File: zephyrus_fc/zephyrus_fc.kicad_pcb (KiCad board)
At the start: 4 copper layers, 92.7 x 43.2 mm, 58 parts, among them J1 SWD_interface, J10 Conn_02x20_Counter_Clockwise, J11 Conn_02x04_Counter_Clockwise, J2 POWER, J3 SERVO1, J4 SERVO2, J5 SERVO3, J6 SERVO4, J7 SERVO5, J8 IBUS_RX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

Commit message: ready to order
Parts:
- added J12: GPS_UART, Connector_PinHeader_2.54mm:PinHeader_1x06_P2.54mm_Vertical, F.Cu at (119.4, 64.0)
- added J13: USART2, Connector_PinHeader_2.54mm:PinHeader_1x06_P2.54mm_Vertical, F.Cu at (123.2, 64.0)
- added J15: Conn_01x04, Connector_PinHeader_2.54mm:PinHeader_1x04_P2.54mm_Vertical, F.Cu at (130.6, 64.0)
- added J16: Conn_01x04, Connector_PinHeader_2.54mm:PinHeader_1x04_P2.54mm_Vertical, F.Cu at (126.8, 64.0)
- added R11: 2.2k, Resistor_SMD:R_0402_1005Metric, F.Cu at (119.9, 57.9)
- added R12: 2.2k, Resistor_SMD:R_0402_1005Metric, F.Cu at (118.6, 57.9)
- added R13: 2.2k, Resistor_SMD:R_0402_1005Metric, F.Cu at (117.3, 57.9)
- added R14: 2.2k, Resistor_SMD:R_0402_1005Metric, F.Cu at (116.1, 57.9)
- added R7: 2.2k, Resistor_SMD:R_0402_1005Metric, F.Cu at (114.8, 57.9)
- added R8: 2.2k, Resistor_SMD:R_0402_1005Metric, F.Cu at (113.5, 57.9)
- moved J5 75.0 mm to (192.0, 63.9), turned to -90 degrees
- moved J3 74.7 mm to (182.4, 63.8), turned to -90 degrees
- moved J6 68.4 mm to (192.0, 68.5), turned to -90 degrees
- moved J4 68.1 mm to (182.4, 68.5), turned to -90 degrees
- moved J7 61.8 mm to (192.0, 73.2), turned to -90 degrees
- moved J8 55.2 mm to (192.0, 77.8), turned to -90 degrees
- moved J2 48.4 mm to (192.0, 82.3), turned to -90 degrees
- moved D1 31.1 mm to (106.4, 87.9)
- moved R2 31.1 mm to (109.2, 87.9)
- moved J1 20.7 mm to (172.2, 73.2), turned to 90 degrees
- moved U5 11.3 mm to (108.0, 65.0), turned to 0 degrees
- moved C26 11.1 mm to (178.8, 75.4), turned to 180 degrees
- moved R6 10.5 mm to (178.8, 76.7), turned to 0 degrees
- moved R5 10.1 mm to (178.8, 78.0), turned to 180 degrees
- moved C23 5.63 mm to (113.6, 66.8), turned to 0 degrees
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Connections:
- net /PB10 renamed /I2C2_SCL
- net /PB11 renamed /I2C2_SDA
- net /PB8 renamed /I2C1_SCL
- net /PB9 renamed /I2C1_SDA
- net /PD12 renamed /I2C4_SCL
- net /PD13 renamed /I2C4_SDA
- net VCC renamed +5V
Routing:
- net +5V: track 17.5 -> 197.9 mm, vias 0 -> 3
- net /I2C1_SCL: track 34.4 -> 100.9 mm
- net /PA8: track 24.3 -> 90.1 mm
- net /PA9: track 20.3 -> 82.9 mm, vias 0 -> 3
- net /I2C1_SDA: track 33.0 -> 92.9 mm, vias 1 -> 2
- net /PC6: track 27.3 -> 84.4 mm, vias 0 -> 3
- net /PA13: track 19.9 -> 74.6 mm, vias 1 -> 2
- net /PA14: track 12.7 -> 67.0 mm, vias 0 -> 2
- net /PC7: track 23.4 -> 76.0 mm, vias 0 -> 3
- net /PE0: track 32.8 -> 73.2 mm, vias 1 -> 3
- net /PB6: track 22.3 -> 60.5 mm
- net /I2C4_SCL: track 31.2 -> 68.9 mm, vias 0 -> 1
- net /PE1: track 30.6 -> 68.1 mm, vias 1 -> 3
- net /I2C2_SCL: track 16.8 -> 53.8 mm
- net /PD3: track 17.4 -> 53.5 mm, vias 0 -> 1
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
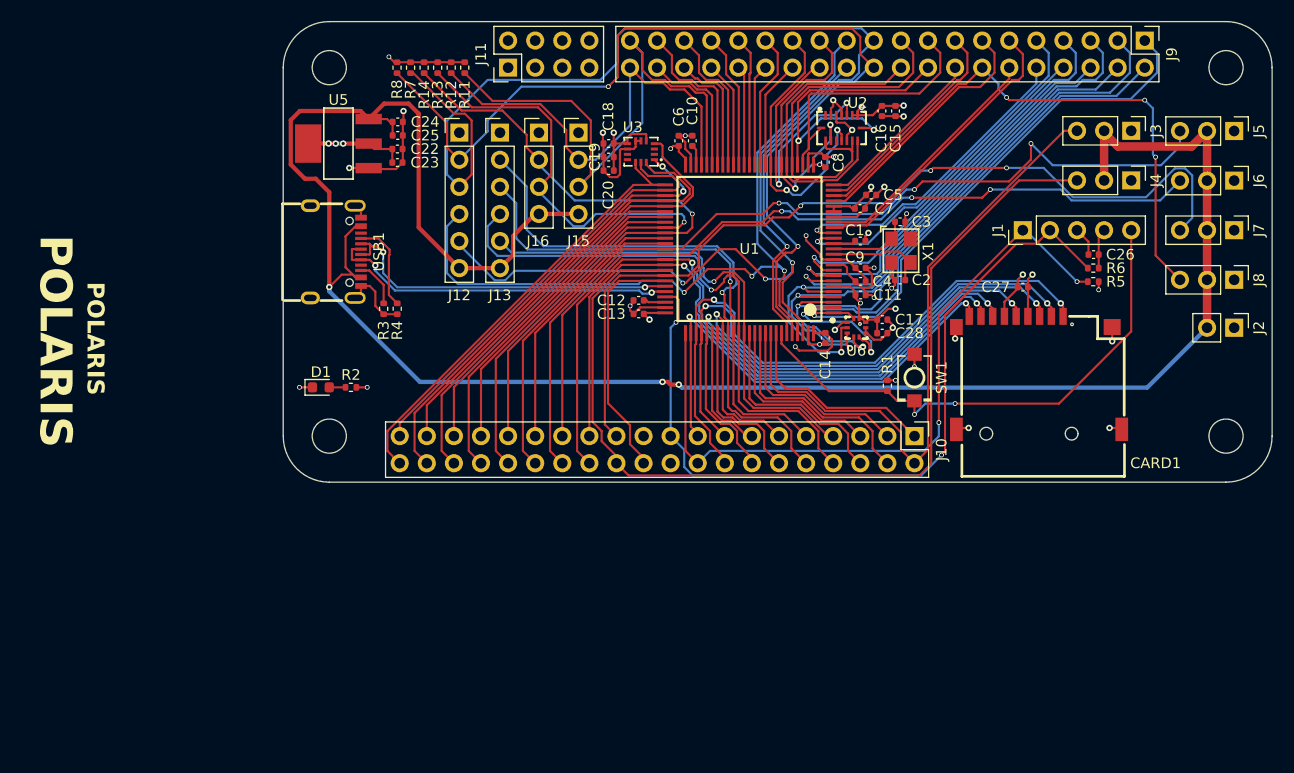
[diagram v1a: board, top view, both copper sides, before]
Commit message: silkscreened
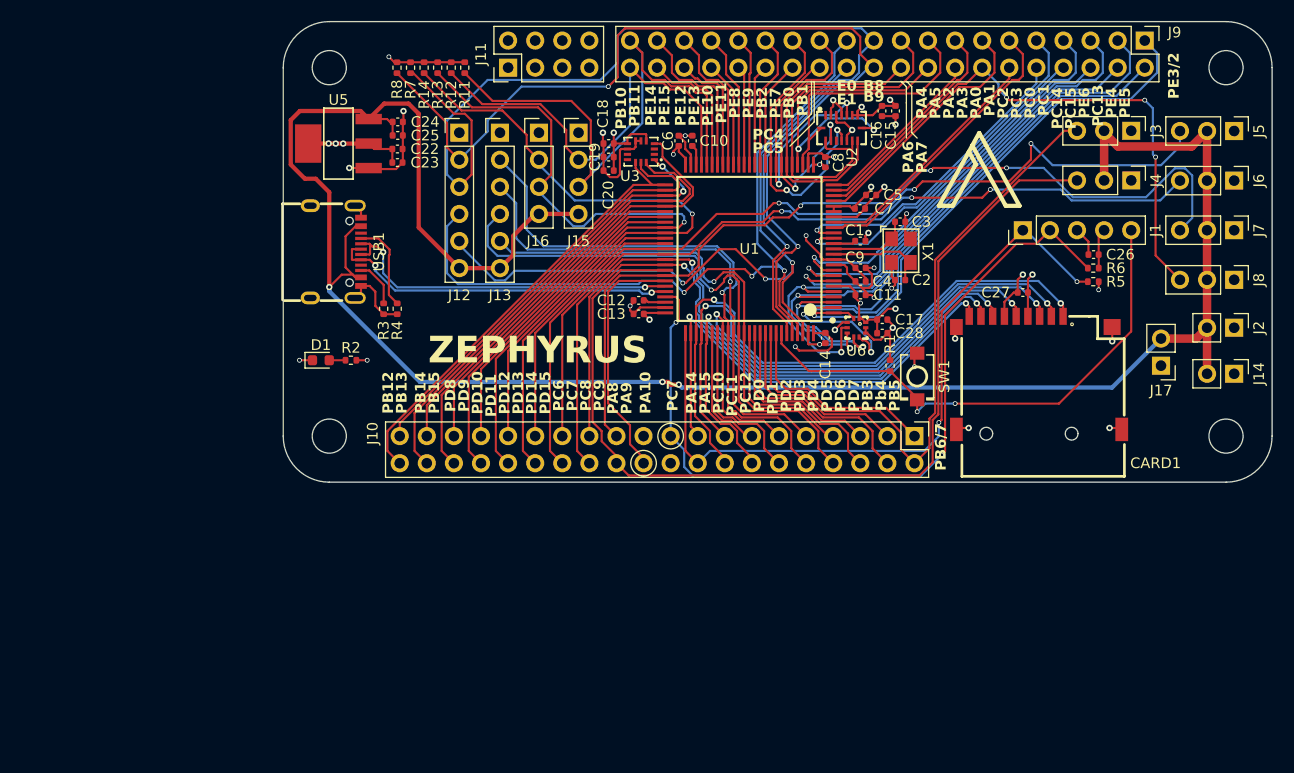
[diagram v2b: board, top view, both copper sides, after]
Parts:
- added J14: POWER, Connector_PinHeader_2.54mm:PinHeader_1x02_P2.54mm_Vertical, F.Cu at (192.0, 86.6)
- added J17: POWER, Connector_PinHeader_2.54mm:PinHeader_1x02_P2.54mm_Vertical, F.Cu at (185.2, 85.9)
- moved D1 2.54 mm to (106.4, 85.3)
- moved R2 2.54 mm to (109.2, 85.3)
- moved R1 1.90 mm to (159.8, 85.9)
- moved C27 0.51 mm to (172.2, 79.0)
- moved SW1 0.27 mm to (162.3, 86.9)
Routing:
- net +5V: track 197.9 -> 202.2 mm
- net GND: track 94.0 -> 96.1 mm, vias 26 -> 25
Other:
- board text added: "AVANINDER.COM"
- board text added: "B8"
- board text added: "B9"
- board text added: "E0"
- board text added: "E1"
- board text added: "PA0"
- board text added: "PA1"
- board text added: "PA10"
- board text added: "PA14"
- board text added: "PA15"
- board text added: "PA2"
- board text added: "PA3"
- board text added: "PA4"
- board text added: "PA5"
- board text added: "PA6"
- board text added: "PA7"
- board text added: "PA8"
- board text added: "PA9"
- board text added: "PB0"
- board text added: "PB1"
- board text added: "PB10"
- board text added: "PB11"
- board text added: "PB12"
- board text added: "PB13"
- board text added: "PB14"
- board text added: "PB15"
- board text added: "PB2"
- board text added: "PB3"
- board text added: "PB5"
- board text added: "PB6/7"
- board text added: "PC0"
- board text added: "PC1"
- board text added: "PC10"
- board text added: "PC11"
- board text added: "PC12"
- board text added: "PC13"
- board text added: "PC14"
- board text added: "PC15"
- board text added: "PC2"
- board text added: "PC3"
- board text added: "PC4"
- board text added: "PC5"
- board text added: "PC6"
- board text added: "PC7"
- board text added: "PC8"
- board text added: "PC9"
- board text added: "PD0"
- board text added: "PD1"
- board text added: "PD10"
- board text added: "PD11"
- board text added: "PD12"
- board text added: "PD13"
- board text added: "PD14"
- board text added: "PD15"
- board text added: "PD2"
- board text added: "PD3"
- board text added: "PD4"
- board text added: "PD5"
- board text added: "PD6"
- board text added: "PD7"
- board text added: "PD8"
- board text added: "PD9"
- board text added: "PE10"
- board text added: "PE11"
- board text added: "PE12"
- board text added: "PE13"
- board text added: "PE14"
- board text added: "PE15"
- board text added: "PE3/2"
- board text added: "PE4"
- board text added: "PE5"
- board text added: "PE6"
- board text added: "PE7"
- board text added: "PE8"
- board text added: "PE9"
- board text added: "Pb4"
- board text added: "ZEPHYRUS"
- board text removed: "POLARIS"
